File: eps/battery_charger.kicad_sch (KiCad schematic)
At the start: 14 parts, among them Q1 BSC028N06LS3, U2 LTC4359-MS8, U4 BQ25185

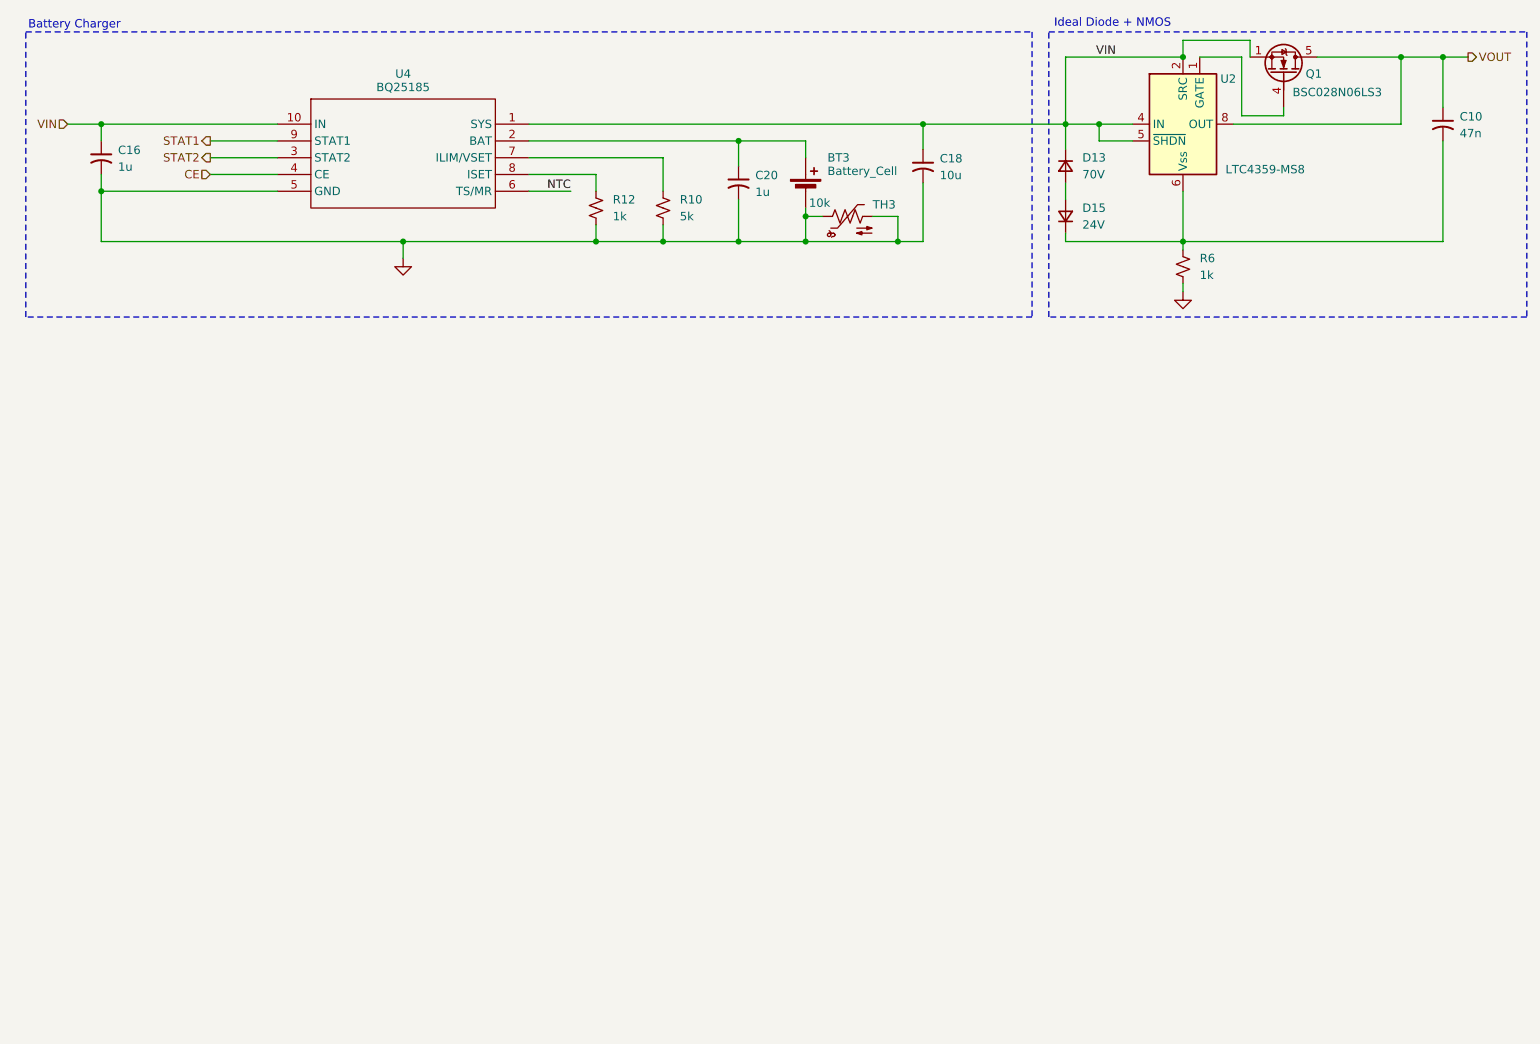
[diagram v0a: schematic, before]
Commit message: start migration away from single-cell charging
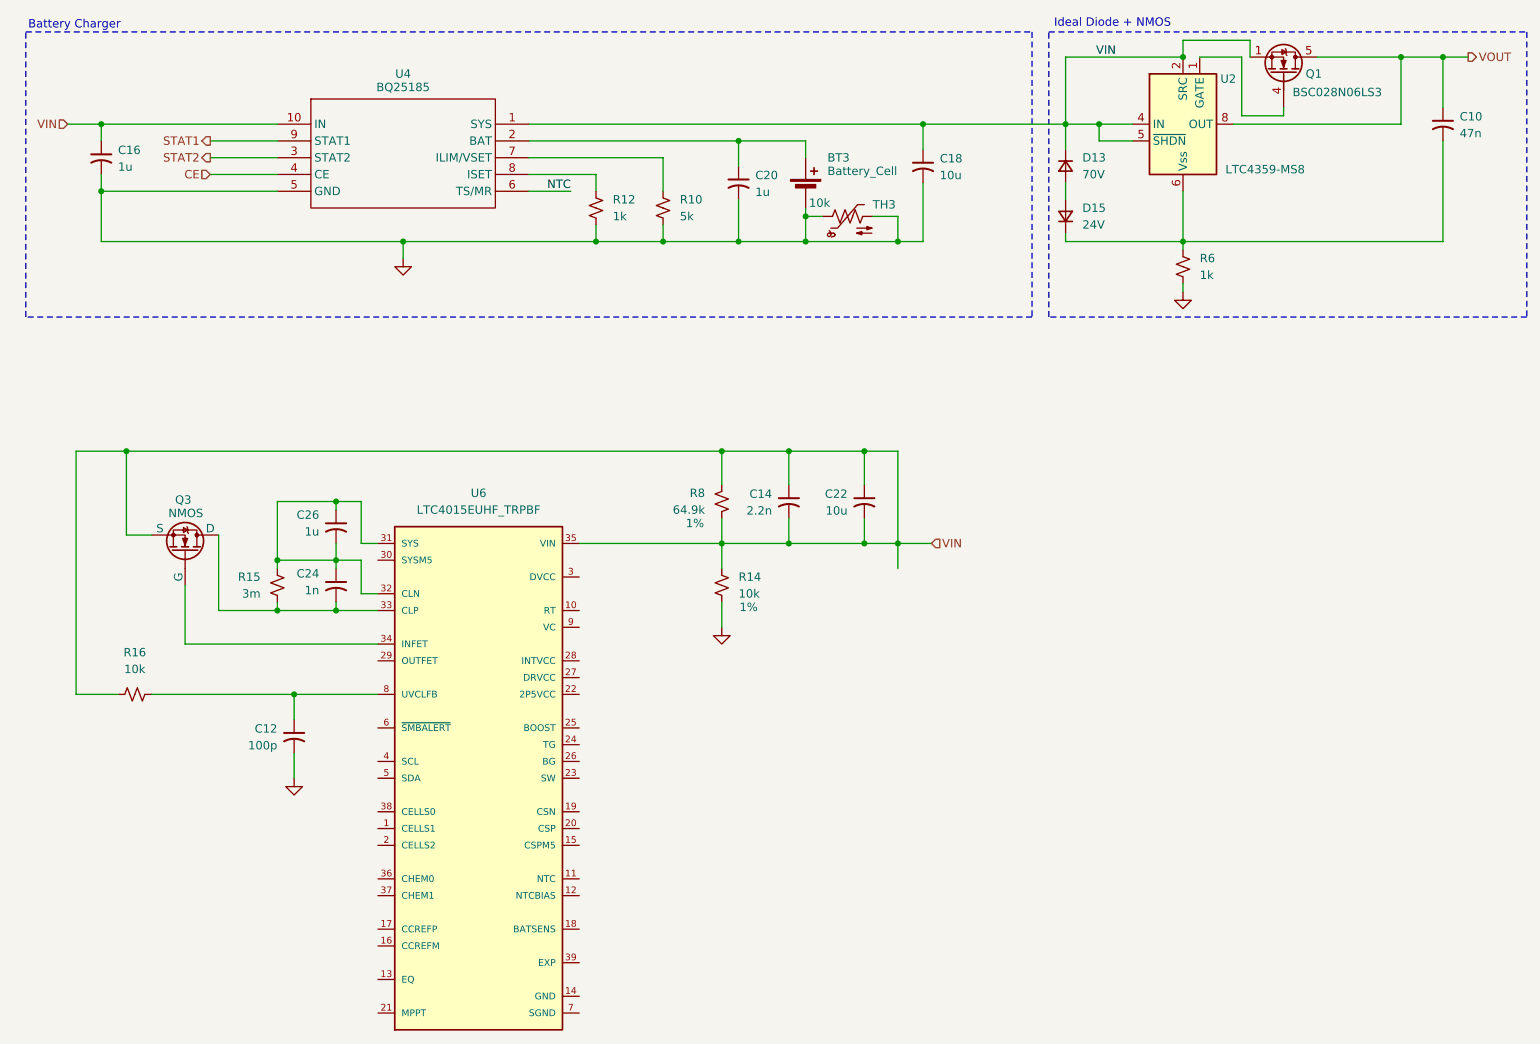
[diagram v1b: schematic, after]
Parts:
- added C12: 100p, symbol Device:C_Small_US
- added C14: 2.2n, symbol Device:C_Small_US
- added C22: 10u, symbol Device:C_Small_US
- added C24: 1n, symbol Device:C_Small_US
- added C26: 1u, symbol Device:C_Small_US
- added Q3: NMOS, symbol Simulation_SPICE:NMOS
- added R14, R16: 10k, symbol Device:R_Small_US
- added R15: 3m, symbol Device:R_Small_US
- added R8: 64.9k, symbol Device:R_Small_US
- added U6: LTC4015EUHF_TRPBF, LTC4015EUHF_TRPBF:QFN50P700X500X80-39N, symbol LTC4015EUHF_TRPBF:LTC4015EUHF_TRPBF
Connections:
- net GND: now also C12.2, R14.2
- net VIN: now also C14.1, C14.2, C22.1, C22.2, Q3.3 (S), R14.1, R16.1, R8.1, R8.2, U6.35 (VIN)
- new net: C12.1, R16.2, U6.8 (UVCLFB)
- new net: C24.2, Q3.1 (D), R15.2, U6.33 (CLP)
- new net: Q3.2 (G), U6.34 (INFET)
- new net: C24.1, C26.1, C26.2, R15.1, U6.31 (SYS), U6.32 (CLN)
